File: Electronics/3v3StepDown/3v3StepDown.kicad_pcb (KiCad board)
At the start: 2 copper layers, 16.3 x 12.7 mm, 5 parts, among them U1 TPS62203DBV, U2 3v3StepDownModule

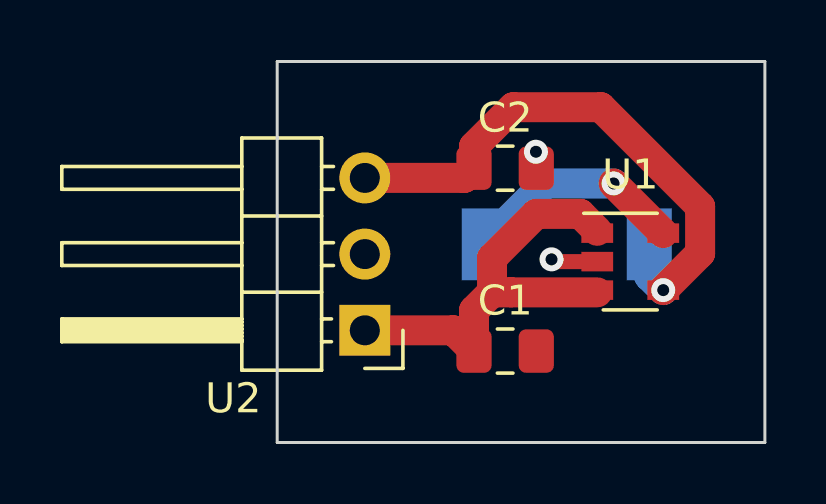
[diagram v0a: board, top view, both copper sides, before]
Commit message: 3v3 boost in dip body
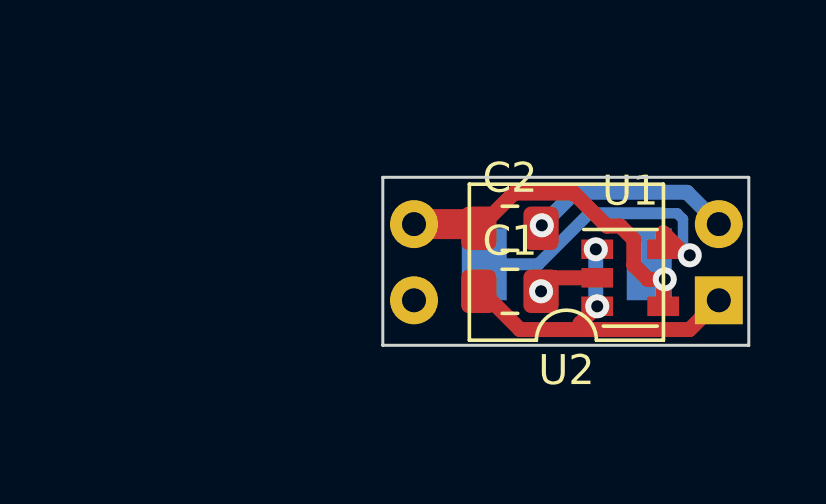
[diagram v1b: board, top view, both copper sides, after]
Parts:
- U2: footprint Connector_PinHeader_2.54mm:PinHeader_1x03_P2.54mm_Horizontal -> Package_DIP:DIP-4_W10.16mm
- moved U2 11.8 mm to (159.5, 86.7)
- moved C2 2.01 mm to (152.5, 84.3)
- moved C1 2.00 mm to (152.5, 86.4)
- moved L1 0.66 mm to (154.4, 85.5)
- moved U1 0.54 mm to (156.5, 86.0)
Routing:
- net +3V3: track 19.0 -> 11.5 mm
- net GND: track 2.11 -> 8.96 mm
- net +5V: track 15.1 -> 12.0 mm, vias 0 -> 2
- net Net-(L1-Pad1): track 7.49 -> 10.5 mm
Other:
- board size 16.3 x 12.7 mm -> 12.2 x 5.6 mm
